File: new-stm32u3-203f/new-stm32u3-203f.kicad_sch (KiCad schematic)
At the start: 25 parts, among them J1 Micro_SD_Card, J2 SJ-3524-SMT, SW1 SW_SPDT, U2 TLV320DAC3203IRGER, U3 STM32U385CGT6Q, X1 32.768kHz

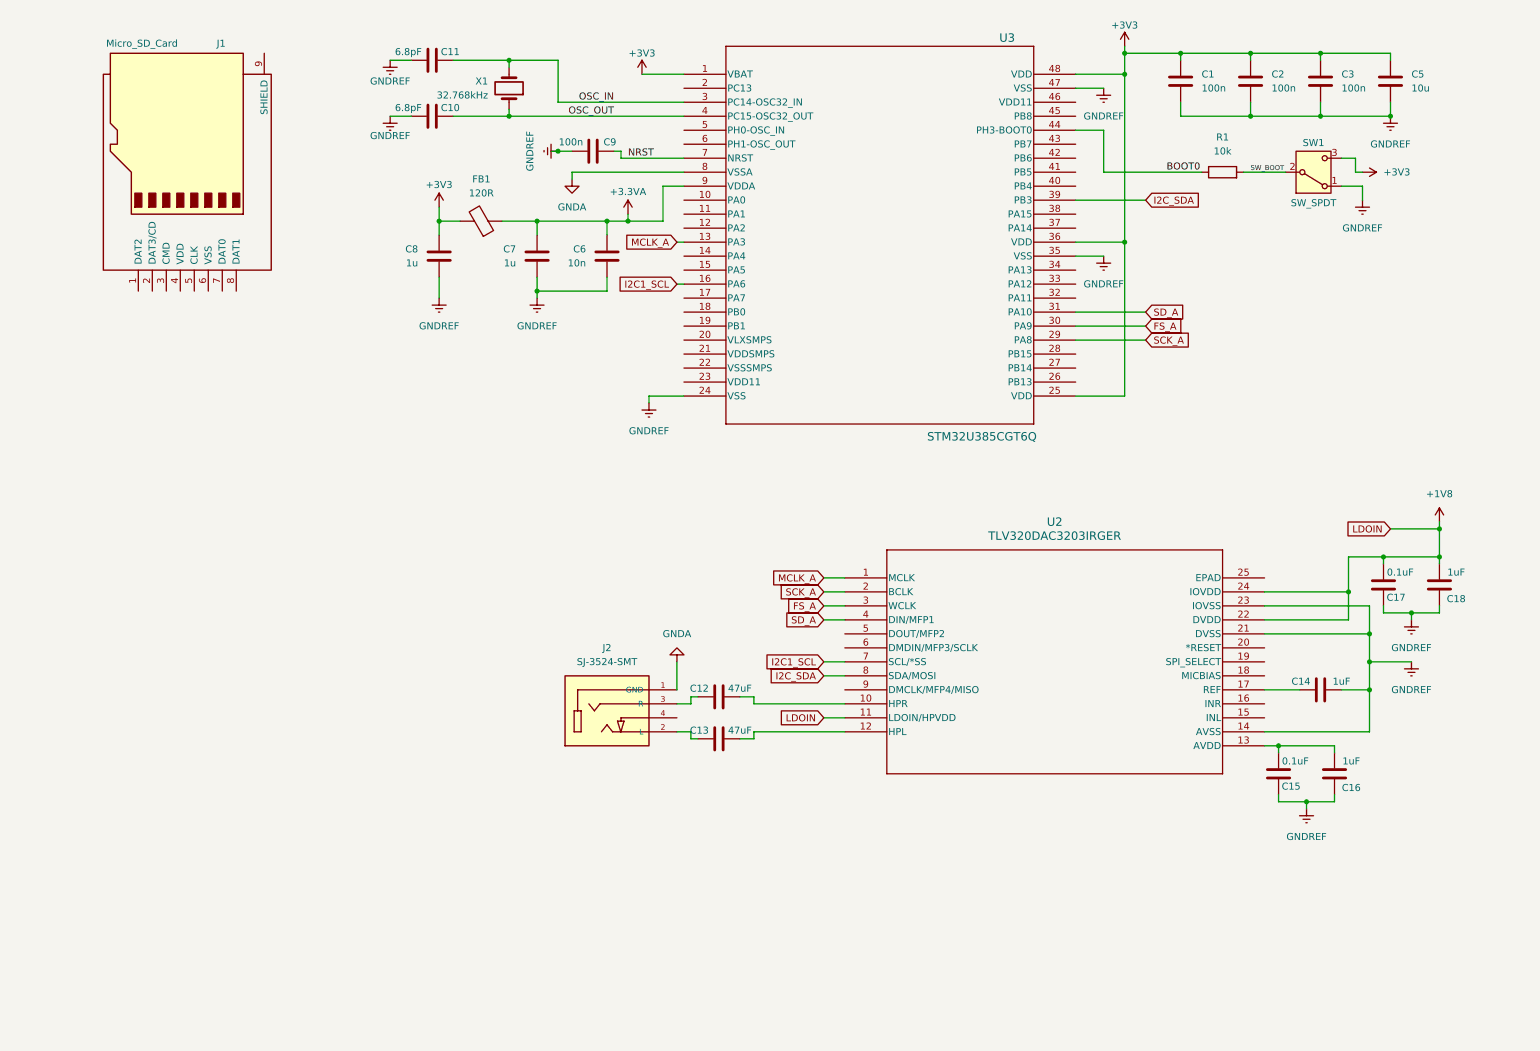
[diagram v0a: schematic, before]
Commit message: added some usb stuff, changed to 64 pinout.
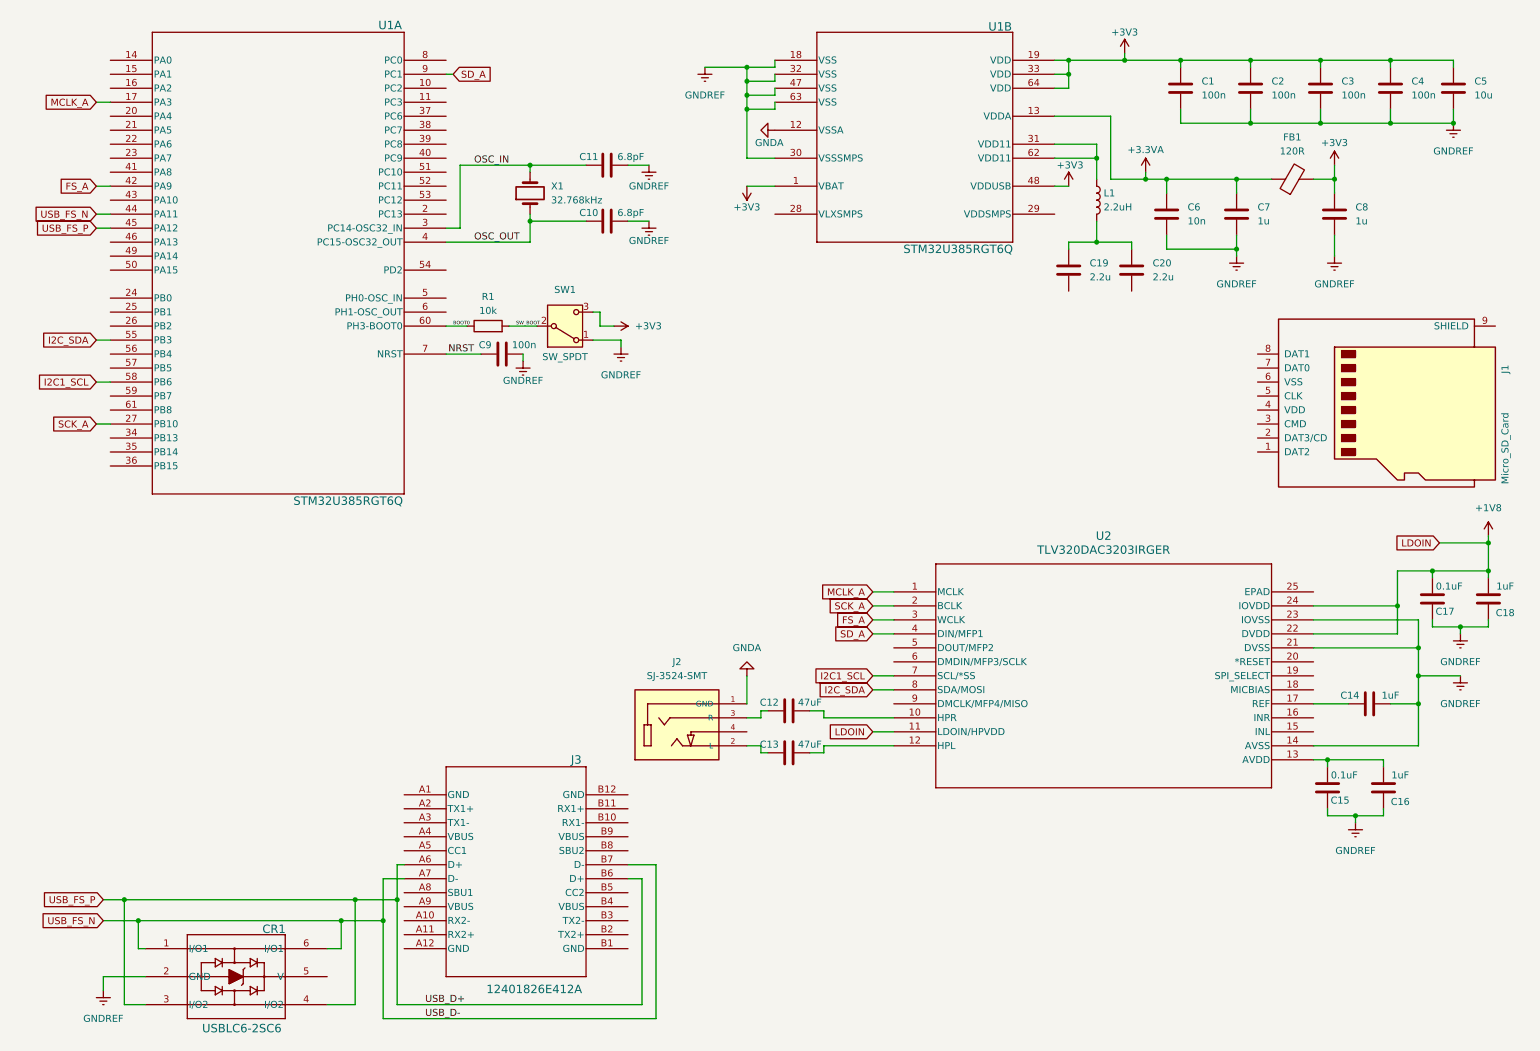
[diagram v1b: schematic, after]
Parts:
- removed U3: STM32U385CGT6Q, LQFP48_7x7_STM, symbol 2026-01-22_07-42-52:STM32U385CGT6Q
- added C19, C20: 2.2u, symbol Device:C
- added C4: 100n, symbol Device:C
- added CR1: USBLC6-2SC6, SOT23-6L_STM, symbol 2026-01-23_08-11-04:USBLC6-2SC6
- added J3: 12401826E412A, 12401826_AMP, symbol 2026-01-23_08-02-34:12401826E412A
- added L1: 2.2uH, symbol Device:L
- added U1: STM32U385RGT6Q, LQFP64_STM, symbol 2026-01-21_08-27-02:STM32U385RGT6Q
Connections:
- net +3.3VA: now also U1.13 (VDDA)
- net +3V3: now also C4.1, U1.1 (VBAT), U1.19 (VDD), U1.33 (VDD), U1.48 (VDDUSB), U1.64 (VDD)
- net BOOT0: now also U1.60 (PH3-BOOT0)
- net FS_A: now also U1.42 (PA9)
- net GNDA: now also U1.12 (VSSA)
- net GNDREF: now also C4.2, CR1.2 (GND), U1.18 (VSS), U1.30 (VSSSMPS), U1.32 (VSS), U1.47 (VSS), U1.63 (VSS)
- net I2C1_SCL: now also U1.58 (PB6)
- net I2C_SDA: now also U1.55 (PB3)
- net MCLK_A: now also U1.17 (PA3)
- net NRST: now also U1.7 (NRST)
- net OSC_IN: now also U1.3 (PC14-OSC32_IN)
- net OSC_OUT: now also U1.4 (PC15-OSC32_OUT)
- net SCK_A: now also U1.27 (PB10)
- net SD_A: now also U1.9 (PC1)
- new net: C19.1, C20.1, L1.2
- new net: L1.1, U1.31 (VDD11), U1.62 (VDD11)
- new net USB_FS_N: CR1.1 (I/O1), CR1.6 (I/O1), J3.A7 (D-), J3.B7 (D-), U1.44 (PA11)
- new net USB_FS_P: CR1.3 (I/O2), CR1.4 (I/O2), J3.A6 (D+), J3.B6 (D+), U1.45 (PA12)
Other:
- moved on the sheet: C1, C10, C11, C12, C13, C14, C15, C16, C17, C18, C2, C3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

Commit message: mcu power finished
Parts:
- removed C19, C20: 2.2u, symbol Device:C
- removed C8: 1u, symbol Device:C
- removed FB1: 120R, symbol Device:FerriteBead
- added C21: 10u, symbol Device:C
- added C22, C23, C24, C25: 100n, symbol Device:C
- added R2: 0R, symbol Device:R
- C1: value 100n -> 1u
- C3, C4: value 100n -> 2.2u
- C6: value 10n -> 100n
- C7: value 1u -> 100n
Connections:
- net +3V3: now also C7.2; no longer C1.1, C2.1, C3.1, C4.1, C5.1, U1.1 (VBAT), U1.19 (VDD), U1.33 (VDD), U1.64 (VDD)
- net GNDA: now also C1.1, C2.1, R2.1
- net GNDREF: now also C5.1, C6.1, C7.1, C21.1, C22.1, C23.1, C24.1, C25.1, R2.2; no longer C1.2, C2.2, C5.2, C6.2, C7.2
- net VLX: now reaches L1.2
- net VLX: now also U1.28 (VLXSMPS)
- net V11: now reaches L1.1, U1.31 (VDD11), U1.62 (VDD11)
- net V11: now also C3.1, C4.1
- net AVDD: now reaches U1.29 (VDDSMPS)
- net AVDD: now also C1.2, C2.2, C5.2, C6.2, U1.1 (VBAT), U1.13 (VDDA), U1.19 (VDD), U1.33 (VDD), U1.64 (VDD), C21.2, C22.2, C23.2, C24.2, C25.2
- removed net +3.3VA: C6.1, C7.1, U1.13 (VDDA)
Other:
- moved on the sheet: CR1, J1, J3, L1

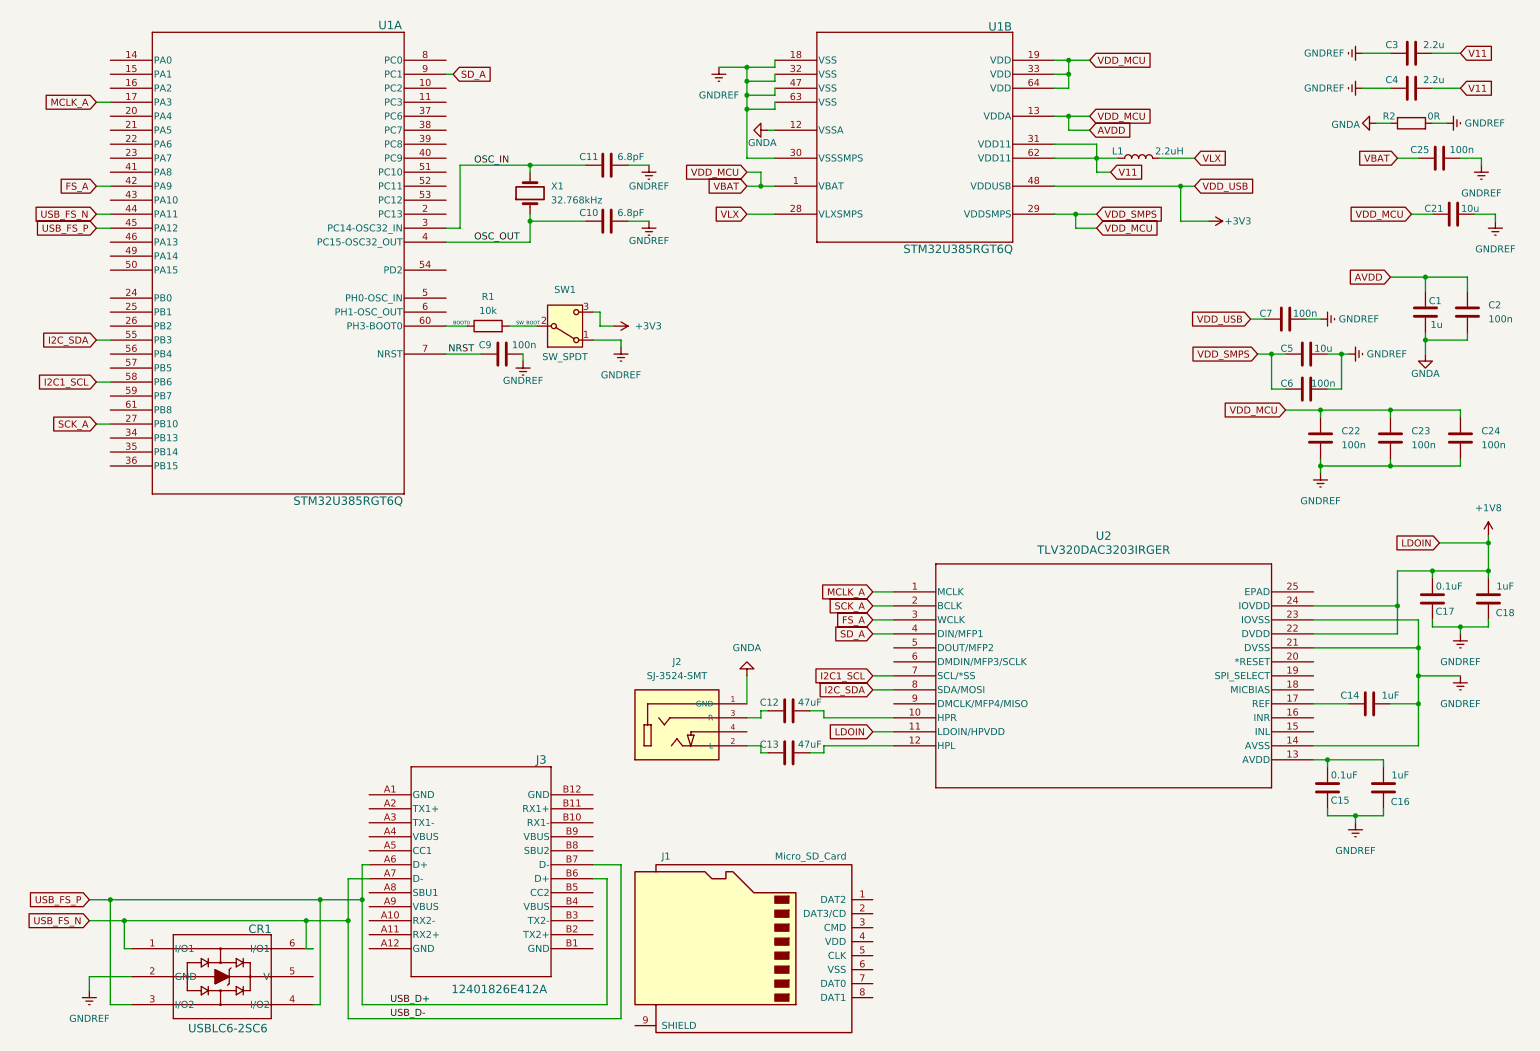
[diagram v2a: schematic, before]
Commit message: finished the sd card wiring up.
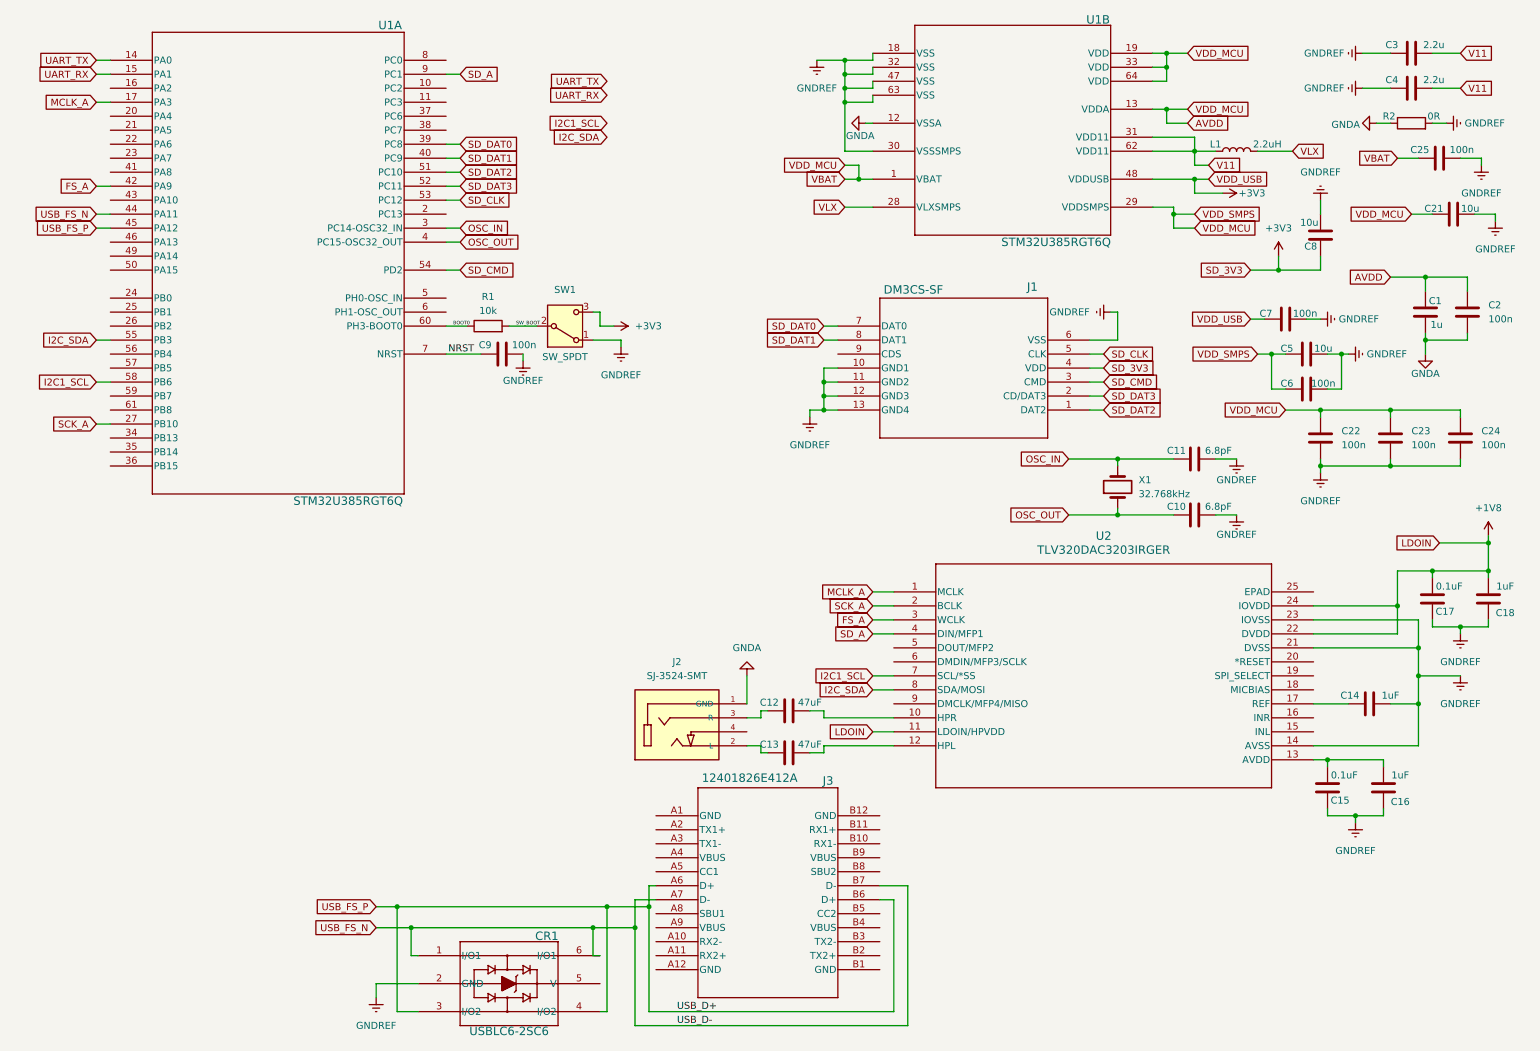
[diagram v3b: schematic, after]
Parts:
- removed J1: Micro_SD_Card, symbol Connector:Micro_SD_Card
- added C8: 10u, symbol Device:C
- added J1: DM3CS-SF, DM3CS-SF_HIR, symbol 2026-01-24_09-53-21:DM3CS-SF
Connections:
- net +3V3: now also C8.2, J1.4 (VDD)
- net GNDREF: now also C8.1, J1.10 (GND1), J1.11 (GND2), J1.12 (GND3), J1.13 (GND4), J1.6 (VSS)
- net UART_TX: now reaches U1.14 (PA0)
- net UART_RX: now reaches U1.15 (PA1)
- net SD_DAT0: now reaches U1.39 (PC8)
- net SD_DAT0: now also J1.7 (DAT0)
- net SD_DAT1: now reaches U1.40 (PC9)
- net SD_DAT1: now also J1.8 (DAT1)
- net SD_DAT2: now reaches U1.51 (PC10)
- net SD_DAT2: now also J1.1 (DAT2)
- net SD_DAT3: now reaches U1.52 (PC11)
- net SD_DAT3: now also J1.2 (CD/DAT3)
- net SD_CLK: now reaches U1.53 (PC12)
- net SD_CLK: now also J1.5 (CLK)
- net SD_CMD: now reaches U1.54 (PD2)
- net SD_CMD: now also J1.3 (CMD)
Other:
- moved on the sheet: C10, C11, CR1, J3, L1, U1B, X1

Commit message: made some prograss on the usb/power stuff.
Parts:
- added C19: 2.2u, symbol Device:C
- added CR2: ESDA25P35-1U1M, QFN1610_STM, symbol 2026-01-24_13-06-26:ESDA25P35-1U1M
- C12, C13: value 47uF -> 47u
- C14, C16, C18: value 1uF -> 1u
- C15, C17: value 0.1uF -> 0.1u
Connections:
- net GNDREF: now also C19.2
- net HP_LEFT: now reaches C13.2, U2.12 (HPL)
- net USB_GND: now reaches J3.A1 (GND)
- net USB_GND: now also J3.A12 (GND), J3.B1 (GND), J3.B12 (GND), CR2.2
- net USB_VBUS: now reaches J3.A4 (VBUS)
- net USB_VBUS: now also J3.A9 (VBUS), J3.B4 (VBUS), J3.B9 (VBUS), C19.1, CR2.1
- net USB_CC1: now reaches J3.A5 (CC1)
- net USB_CC2: now reaches J3.B5 (CC2)
- net HP_RIGHT: now reaches C12.2, U2.10 (HPR)
- net USB_FS_N renamed USB_D-
- net USB_FS_P renamed UBS_D+
- no-connect marks 0 -> 15
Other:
- moved on the sheet: C12, C13, CR1, J2, J3

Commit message: made some progress on the board.
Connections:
- net GNDA: no longer J2.1 (GND)
- net GNDREF: now also J2.1 (GND)
- net DAC_RST: now reaches U2.20 (*RESET)
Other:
- moved on the sheet: C10, C11, C12, C13, C14, C15, C16, C17, C18, J2, U2, X1
